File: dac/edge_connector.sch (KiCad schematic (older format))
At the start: 1 part, among them P1 my_pcie_8x

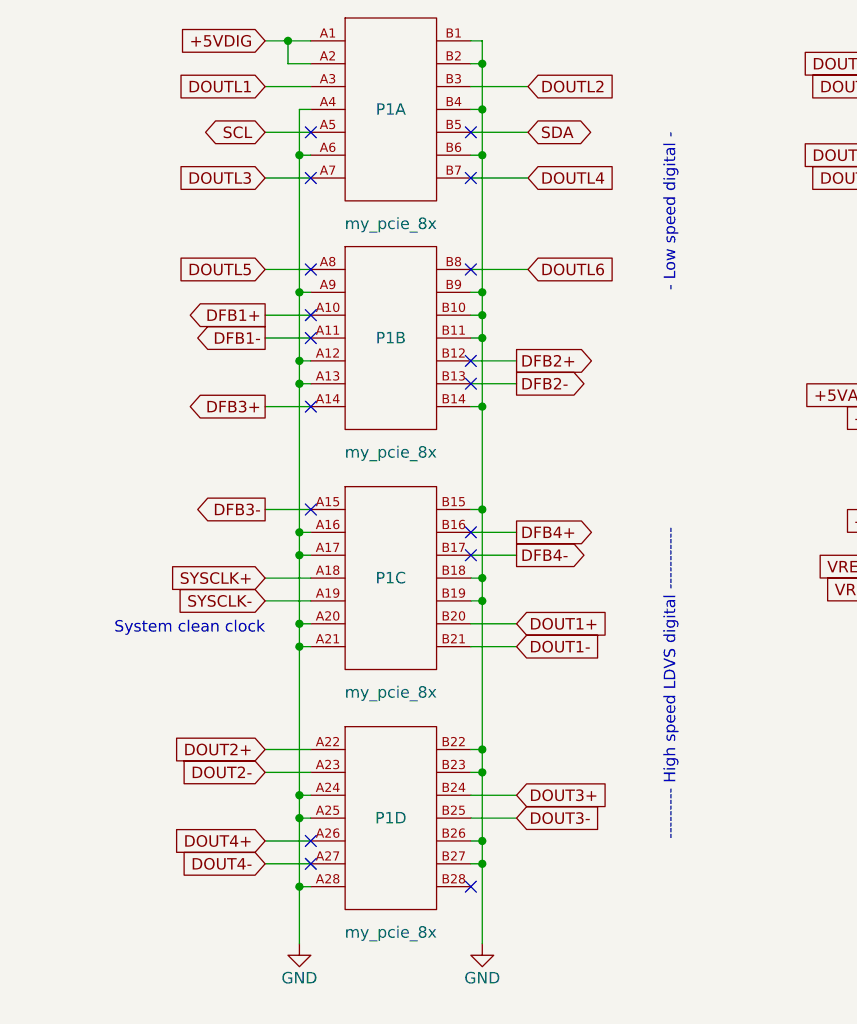
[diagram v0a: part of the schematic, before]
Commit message: DAC board is routed.  I also changed the digital interface to use a buffer (like I did on the input board) so that everything is buffered and we don't have multi-drop nets.
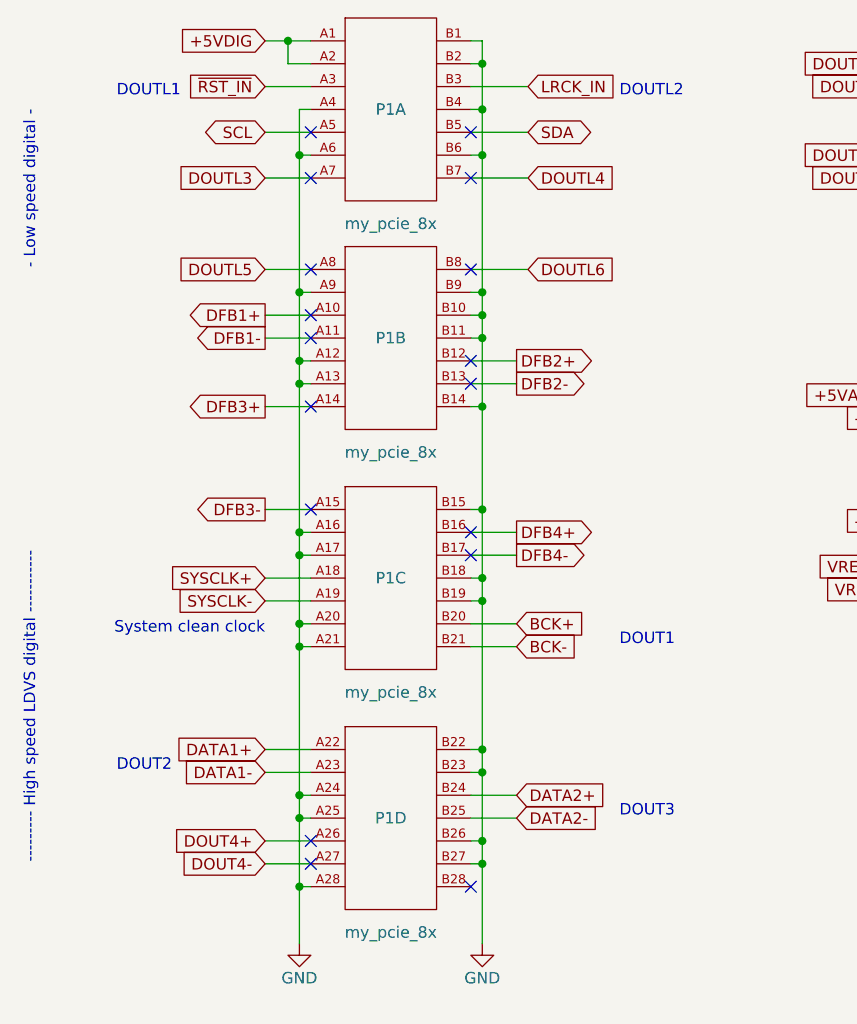
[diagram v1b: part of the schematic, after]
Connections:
- net DOUT1+ renamed BCK+
- net DOUT1- renamed BCK-
- net DOUT2+ renamed DATA1+
- net DOUT2- renamed DATA1-
- net DOUT3+ renamed DATA2+
- net DOUT3- renamed DATA2-
- net DOUTL1 renamed ~RST_IN
- net DOUTL2 renamed LRCK_IN
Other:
- note added: "DOUT1"
- note added: "DOUT2"
- note added: "DOUT3"
- note added: "DOUTL1"
- note added: "DOUTL2"
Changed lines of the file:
@@
 	2600 5200 2600 5450
 Text GLabel 3600 1700 2    50   Input ~ 0
-DOUTL2
+LRCK_IN
 Text GLabel 3600 2100 2    50   Input ~ 0
 DOUTL4
@@
 Text GLabel 3550 3750 2    50   Output ~ 0
 DFB4-
-Text GLabel 3550 4050 2    50   Input ~ 0
-DOUT1+
-Text GLabel 3550 4150 2    50   Input ~ 0
-DOUT1-
-Text GLabel 3550 4800 2    50   Input ~ 0
-DOUT3+
-Text GLabel 3550 4900 2    50   Input ~ 0
-DOUT3-
 Wire Wire Line
 	5400 1500 5400 1800
@@
 Wire Wire Line
 	6300 2950 6300 3050
-Text GLabel 2450 4600 0    50   Input ~ 0
-DOUT2+
-Text GLabel 2450 4700 0    50   Input ~ 0
-DOUT2-
 Text GLabel 2450 5000 0    50   Input ~ 0
 DOUT4+
@@
 DOUTL3
 Text GLabel 2450 1700 0    50   Input ~ 0
-DOUTL1
+~RST_IN
 Text GLabel 2450 1500 0    50   Input ~ 0
 +5VDIG
@@
 Wire Wire Line
 	6300 3050 6300 3700
-Text Notes 4250 5000 1    50   ~ 0
+Text Notes 1450 5100 1    50   ~ 0
 --------- High speed LDVS digital -----------
-Text Notes 4250 2600 1    50   ~ 0
+Text Notes 1450 2500 1    50   ~ 0
 - Low speed digital -
 Text Notes 7050 3600 1    50   ~ 0
@@
 NoConn ~ 6200 2650
 NoConn ~ 2650 3550
+Text GLabel 3550 4050 2    50   Input ~ 0
+BCK+
+Text GLabel 3550 4800 2    50   Input ~ 0
+DATA2+
+Text GLabel 3550 4900 2    50   Input ~ 0
+DATA2-
+Text GLabel 2450 4600 0    50   Input ~ 0
+DATA1+
+Text GLabel 2450 4700 0    50   Input ~ 0
+DATA1-
+Text GLabel 3550 4150 2    50   Input ~ 0
+BCK-
+Text Notes 4000 4150 0    50   ~ 0
+DOUT1
+Text Notes 1800 4700 0    50   ~ 0
+DOUT2
+Text Notes 4000 4900 0    50   ~ 0
+DOUT3
+Text Notes 1800 1750 0    50   ~ 0
+DOUTL1
+Text Notes 4000 1750 0    50   ~ 0
+DOUTL2
 $EndSCHEMATC

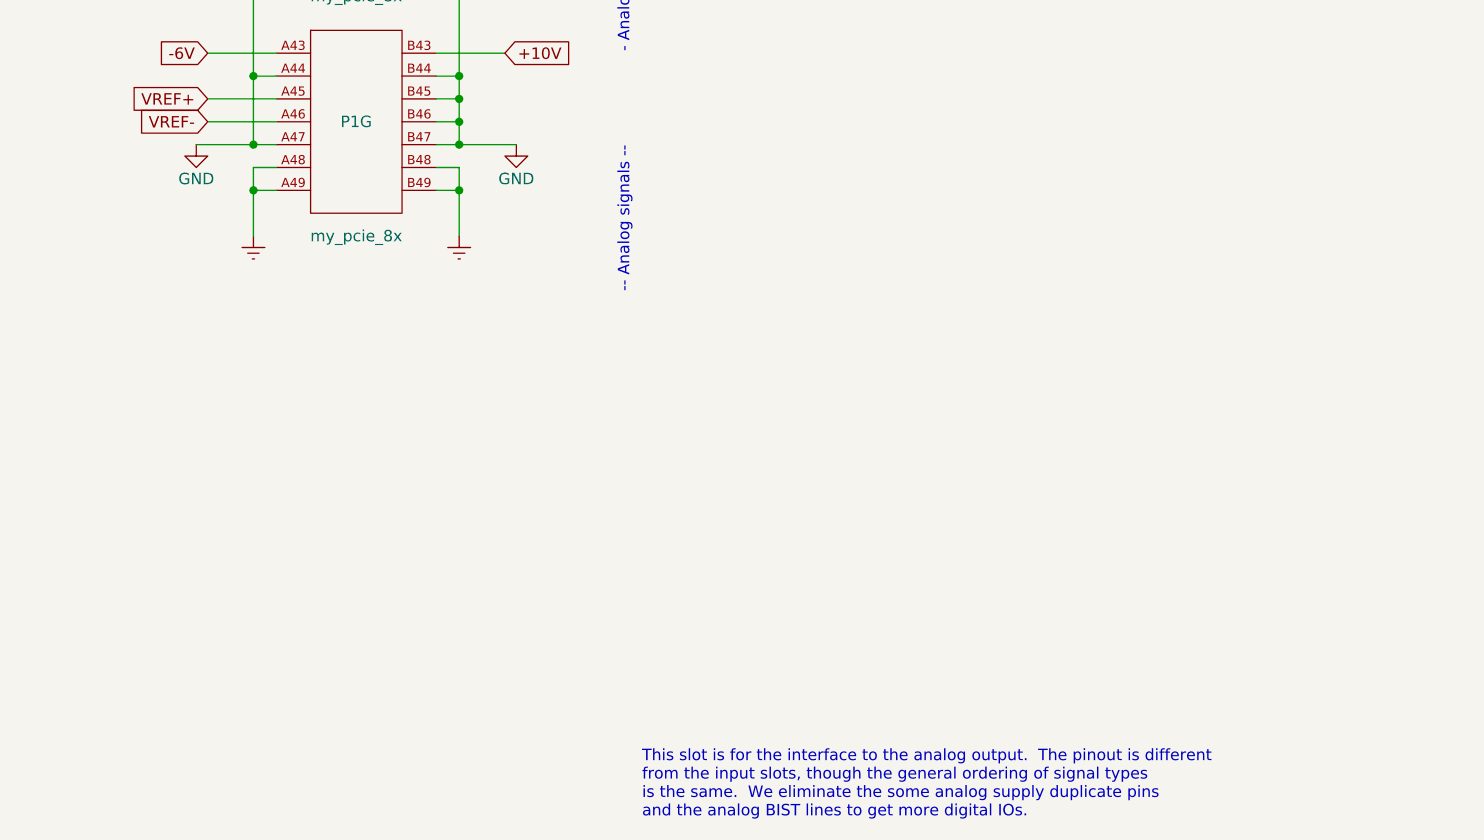
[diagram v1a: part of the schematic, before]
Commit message: Everything seems ready to go for the DAC board.  Made my BOM and checked it twice. Checked footprints of new components and fixed J5, R7-R10.
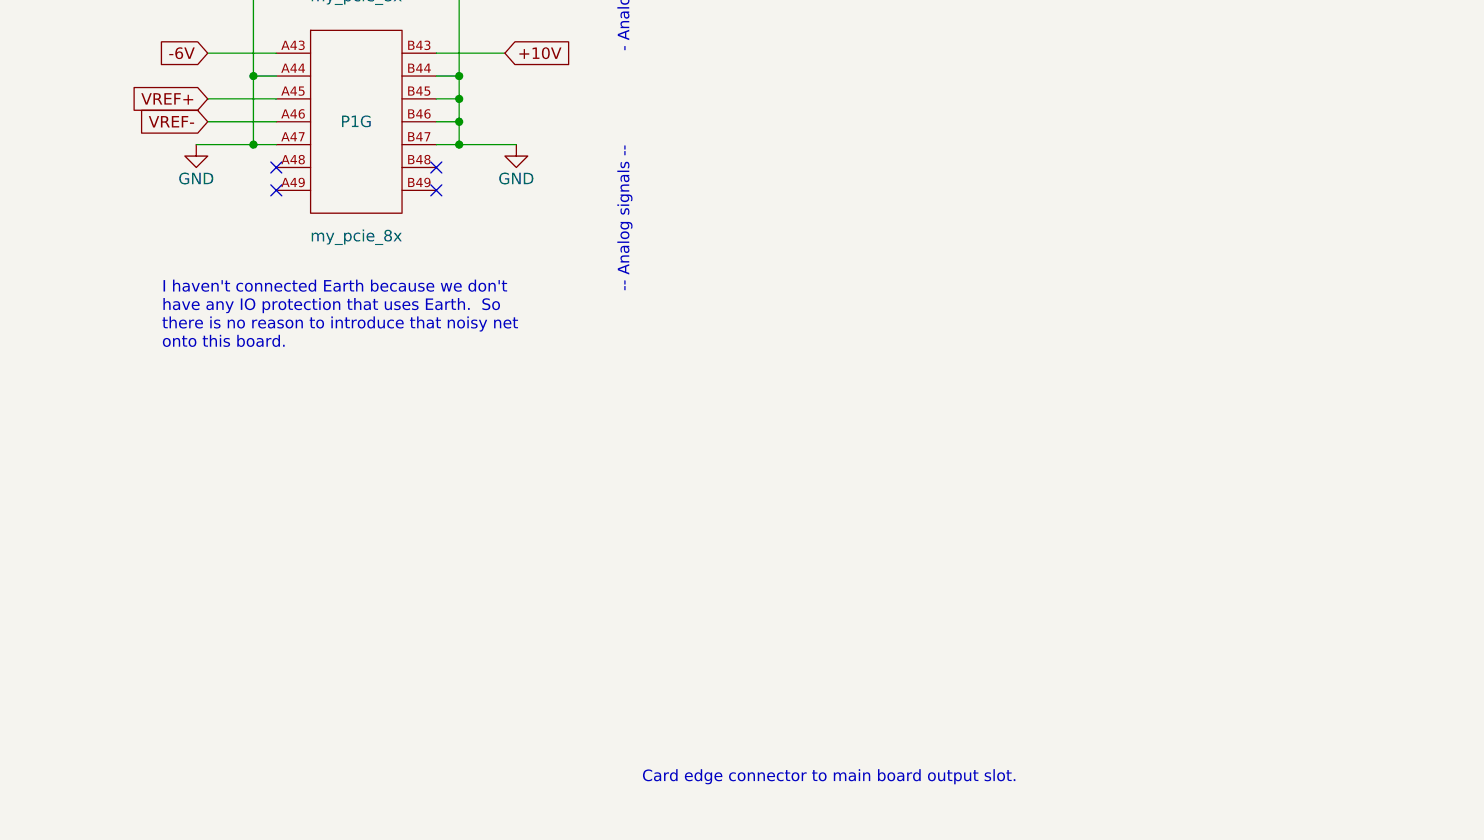
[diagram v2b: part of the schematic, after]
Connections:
- removed net Earth: P1.A48 (A47), P1.A49, P1.B48, P1.B49
- no-connect marks 26 -> 30
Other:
- note added: "Card edge connector to main board output slot."
- note added: "I haven't connected Earth because we don't\nhave any IO protection that uses Earth. So \nthere is no reason to introduce that noisy net\nonto this board.\n"
- note removed: "This slot is for the interface to the analog output. The pinout is different\nfrom the input slots, though the general ordering of signal types\nis the same. We eliminate the some analog supply duplicate pins\nand the analog BIST lines to get more digital IOs."
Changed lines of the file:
@@
 Comment4 ""
 $EndDescr
-Text Notes 7100 6950 0    50   ~ 0
-This slot is for the interface to the analog output.  The pinout is different\nfrom the input slots, though the general ordering of signal types\nis the same.  We eliminate the some analog supply duplicate pins\nand the analog BIST lines to get more digital IOs.
+Text Notes 7100 6800 0    50   ~ 0
+Card edge connector to main board output slot.
 Text GLabel 5200 3800 0    50   Input ~ 0
 VREF+
@@
 Wire Wire Line
 	2550 1500 2650 1500
-$Comp
-L power:Earth #PWR?
-U 1 1 5EC152AA
-P 6300 4400
-AR Path="/5E51E83D/5EC152AA" Ref="#PWR?"  Part="1"
-AR Path="/5E1D6729/5EC152AA" Ref="#PWR?"  Part="1"
-AR Path="/5E525F2C/5E59D3A2/5EC152AA" Ref="#PWR?"  Part="1"
-AR Path="/5E525F2C/5E76A42A/5EC152AA" Ref="#PWR?"  Part="1"
-AR Path="/5E525F2C/5E76E218/5EC152AA" Ref="#PWR?"  Part="1"
-AR Path="/5E525F2C/5E7721D1/5EC152AA" Ref="#PWR?"  Part="1"
-AR Path="/5E525FFE/5EBAAEAF/5EC152AA" Ref="#PWR?"  Part="1"
-AR Path="/5E525FFE/5EBAAF7D/5EC152AA" Ref="#PWR?"  Part="1"
-AR Path="/5E525FFE/5EBAAF8F/5EC152AA" Ref="#PWR?"  Part="1"
-AR Path="/5E525FFE/5EBAAFA1/5EC152AA" Ref="#PWR?"  Part="1"
-AR Path="/5EC15224/5EC152AA" Ref="#PWR?"  Part="1"
-AR Path="/5F801832/5EC152AA" Ref="#PWR0119"  Part="1"
-F 0 "#PWR0119" H 6300 4150 50  0001 C CNN
-F 1 "Earth" H 6300 4250 50  0001 C CNN
-F 2 "" H 6300 4400 50  0001 C CNN
-F 3 "~" H 6300 4400 50  0001 C CNN
-	1    6300 4400
-	1    0    0    -1
-$EndComp
-Wire Wire Line
-	6200 4100 6300 4100
-Wire Wire Line
-	6300 4100 6300 4200
-Wire Wire Line
-	6200 4200 6300 4200
-Connection ~ 6300 4200
-Wire Wire Line
-	6300 4200 6300 4400
-$Comp
-L power:Earth #PWR?
-U 1 1 5EC152AB
-P 5400 4400
-AR Path="/5E51E83D/5EC152AB" Ref="#PWR?"  Part="1"
-AR Path="/5E1D6729/5EC152AB" Ref="#PWR?"  Part="1"
-AR Path="/5E525F2C/5E59D3A2/5EC152AB" Ref="#PWR?"  Part="1"
-AR Path="/5E525F2C/5E76A42A/5EC152AB" Ref="#PWR?"  Part="1"
-AR Path="/5E525F2C/5E76E218/5EC152AB" Ref="#PWR?"  Part="1"
-AR Path="/5E525F2C/5E7721D1/5EC152AB" Ref="#PWR?"  Part="1"
-AR Path="/5E525FFE/5EBAAEAF/5EC152AB" Ref="#PWR?"  Part="1"
-AR Path="/5E525FFE/5EBAAF7D/5EC152AB" Ref="#PWR?"  Part="1"
-AR Path="/5E525FFE/5EBAAF8F/5EC152AB" Ref="#PWR?"  Part="1"
-AR Path="/5E525FFE/5EBAAFA1/5EC152AB" Ref="#PWR?"  Part="1"
-AR Path="/5EC15224/5EC152AB" Ref="#PWR?"  Part="1"
-AR Path="/5F801832/5EC152AB" Ref="#PWR0120"  Part="1"
-F 0 "#PWR0120" H 5400 4150 50  0001 C CNN
-F 1 "Earth" H 5400 4250 50  0001 C CNN
-F 2 "" H 5400 4400 50  0001 C CNN
-F 3 "~" H 5400 4400 50  0001 C CNN
-	1    5400 4400
-	1    0    0    -1
-$EndComp
-Wire Wire Line
-	5400 4400 5400 4200
-Wire Wire Line
-	5400 4200 5500 4200
-Wire Wire Line
-	5500 4100 5400 4100
-Wire Wire Line
-	5400 4100 5400 4200
-Connection ~ 5400 4200
 Wire Wire Line
 	6550 4000 6300 4000
@@
 Text Notes 4000 1750 0    50   ~ 0
 DOUTL2
+NoConn ~ 6200 4100
+NoConn ~ 6200 4200
+NoConn ~ 5500 4200
+NoConn ~ 5500 4100
+Text Notes 5000 4900 0    50   ~ 0
+I haven't connected Earth because we don't\nhave any IO protection that uses Earth.  So \nthere is no reason to introduce that noisy net\nonto this board.\n
 $EndSCHEMATC
